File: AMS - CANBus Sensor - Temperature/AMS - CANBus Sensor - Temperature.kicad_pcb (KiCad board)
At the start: 2 copper layers, 72.9 x 71.1 mm, 45 parts, among them IC2 OPA4340UA, J1 Power_And_CAN, J2 Power_And_CAN, J3 TTL_Programmer, J4 ICSP, J5 Conn_01x02, J6 Screw_Terminal_01x02, Q1 IRF9Z34NPBF, U1 3568, U2 ATmega328P-P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

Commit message: wip for the temp sensor
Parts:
- removed IC2: OPA4340UA, SamacSys_Parts:SOIC127P600X175-14N
- removed J2: Power_And_CAN, TerminalBlock_Phoenix:TerminalBlock_Phoenix_MPT-0,5-4-2.54_1x04_P2.54mm_Horizontal
- removed J6: Screw_Terminal_01x02, TerminalBlock_Phoenix:TerminalBlock_Phoenix_MPT-0,5-2-2.54_1x02_P2.54mm_Horizontal
- removed R10, R11, R12, R13: 47K, Resistor_SMD:R_1206_3216Metric_Pad1.30x1.75mm_HandSolder
- removed R14, R15, R8, R9: 100K, Resistor_SMD:R_1206_3216Metric_Pad1.30x1.75mm_HandSolder
- removed RV1, RV2, RV3, RV4: 200k, Potentiometer_THT:Potentiometer_Bourns_3296W_Vertical
- removed U1: 3568, SamacSys_Parts:3568
- added C41: 0.33uF, Capacitor_SMD:C_1206_3216Metric_Pad1.33x1.80mm_HandSolder, F.Cu at (79.3, 73.2)
- added C42: 0.33uF, Capacitor_SMD:C_1206_3216Metric_Pad1.33x1.80mm_HandSolder, F.Cu at (79.3, 76.6)
- added C43: 100nF, Capacitor_SMD:C_1206_3216Metric_Pad1.33x1.80mm_HandSolder, F.Cu at (79.3, 79.9)
- added IC18: MAX31865AAP+, SamacSys_Parts:SOP65P778X199-20N, F.Cu at (87.4, 76.0)
- added J28: Conn_01x02, Connector_PinHeader_2.54mm:PinHeader_1x02_P2.54mm_Vertical, F.Cu at (84.6, 82.8)
- added J29: Conn_01x03, Connector_PinHeader_2.54mm:PinHeader_1x03_P2.54mm_Vertical, F.Cu at (78.6, 83.9)
- added J30: Conn_01x02, Connector_PinHeader_2.54mm:PinHeader_1x02_P2.54mm_Vertical, F.Cu at (89.3, 82.8)
- added R60: 430, Resistor_THT:R_Axial_DIN0207_L6.3mm_D2.5mm_P2.54mm_Vertical, F.Cu at (84.3, 89.7)
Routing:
- net GND: track 276.6 -> 0.00 mm, vias 2 -> 0
- net +5V: track 185.4 -> 0.00 mm, vias 2 -> 0
- net /BufferedADC/ADCIN4: track 98.9 -> 0.00 mm, vias 1 -> 0
- net /BareMinAtmel328P/PB3-D11-MOSI: track 98.5 -> 0.00 mm, vias 1 -> 0
- net /BareMinAtmel328P/PB1-D9: track 92.8 -> 0.00 mm, vias 2 -> 0
- net /BareMinAtmel328P/RESET: track 92.4 -> 0.00 mm, vias 4 -> 0
- net /BareMinAtmel328P/PC3-A3: track 78.5 -> 0.00 mm, vias 2 -> 0
- net Net-(U3-OSC1): track 77.0 -> 0.00 mm
- net /BareMinAtmel328P/PB5-D13-SCK: track 75.2 -> 0.00 mm, vias 2 -> 0
- net Net-(U3-OSC2): track 72.5 -> 0.00 mm
- net /BufferedADC/ADCIN3: track 58.3 -> 0.00 mm, vias 1 -> 0
- net /BareMinAtmel328P/PB4-D12-MISO: track 53.7 -> 0.00 mm, vias 2 -> 0
- net /BareMinAtmel328P/PC1-A1: track 51.2 -> 0.00 mm, vias 2 -> 0
- net /BareMinAtmel328P/PC2-A2: track 46.0 -> 0.00 mm, vias 3 -> 0
- net /BufferedADC/ADCIN2: track 45.2 -> 0.00 mm, vias 2 -> 0
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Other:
- board text added: "AMS CANBus RTD Temp V1.0 Rev A"
- board text removed: "1 Amp 5V"
- board text removed: "AMS CANBus Voltage V1.0 Rev A"
- board text removed: "Fused"

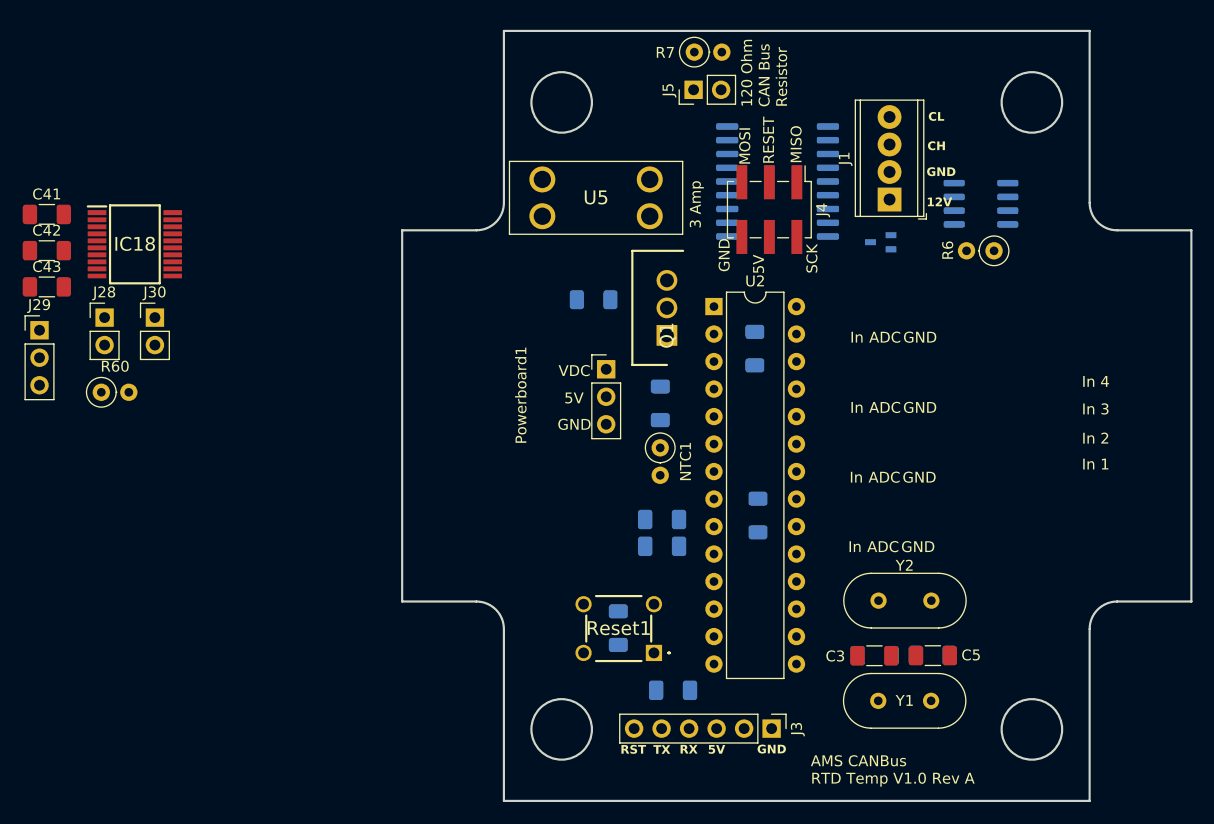
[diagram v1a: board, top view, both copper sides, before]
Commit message: Temp Sensor Done
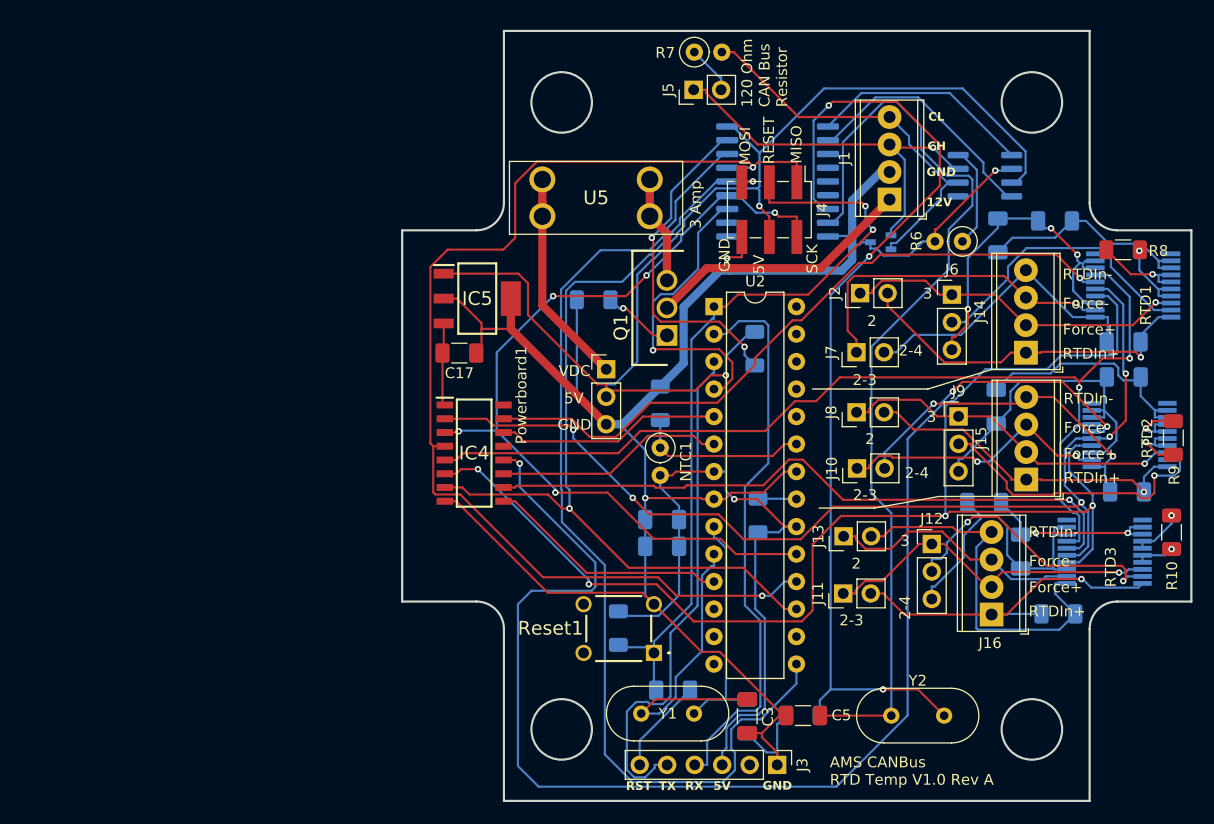
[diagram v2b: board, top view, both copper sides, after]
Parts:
- removed C41, C42: 0.33uF, Capacitor_SMD:C_1206_3216Metric_Pad1.33x1.80mm_HandSolder
- removed C43: 100nF, Capacitor_SMD:C_1206_3216Metric_Pad1.33x1.80mm_HandSolder
- removed IC18: MAX31865AAP+, SamacSys_Parts:SOP65P778X199-20N
- removed J28, J30: Conn_01x02, Connector_PinHeader_2.54mm:PinHeader_1x02_P2.54mm_Vertical
- removed J29: Conn_01x03, Connector_PinHeader_2.54mm:PinHeader_1x03_P2.54mm_Vertical
- removed R60: 430, Resistor_THT:R_Axial_DIN0207_L6.3mm_D2.5mm_P2.54mm_Vertical
- added C10: 100nF, Capacitor_SMD:C_1206_3216Metric_Pad1.33x1.80mm_HandSolder, B.Cu at (178.8, 85.0)
- added C11: 0.33uF, Capacitor_SMD:C_1206_3216Metric_Pad1.33x1.80mm_HandSolder, B.Cu at (178.8, 88.3)
- added C12: 0.33uF, Capacitor_SMD:C_1206_3216Metric_Pad1.33x1.80mm_HandSolder, B.Cu at (167.0, 91.0)
- added C13: 100nF, Capacitor_SMD:C_1206_3216Metric_Pad1.33x1.80mm_HandSolder, B.Cu at (179.1, 98.9)
- added C14: 0.33uF, Capacitor_SMD:C_1206_3216Metric_Pad1.33x1.80mm_HandSolder, B.Cu at (165.9, 99.9)
- added C15: 0.33uF, Capacitor_SMD:C_1206_3216Metric_Pad1.33x1.80mm_HandSolder, B.Cu at (169.3, 104.4)
- added C16: 100nF, Capacitor_SMD:C_1206_3216Metric_Pad1.33x1.80mm_HandSolder, B.Cu at (172.7, 110.1)
- added C17: 22uf, Capacitor_SMD:C_1206_3216Metric_Pad1.33x1.80mm_HandSolder, F.Cu at (117.4, 86.1)
- added C8: 0.33uF, Capacitor_SMD:C_1206_3216Metric_Pad1.33x1.80mm_HandSolder, B.Cu at (167.2, 75.2)
- added C9: 0.33uF, Capacitor_SMD:C_1206_3216Metric_Pad1.33x1.80mm_HandSolder, B.Cu at (172.4, 73.8)
- added IC1: MAX31865AAP+, SamacSys_Parts:SOP65P778X199-20N, B.Cu at (179.7, 79.8)
- added IC2: MAX31865AAP+, SamacSys_Parts:SOP65P778X199-20N, B.Cu at (179.3, 93.6)
- added IC3: MAX31865AAP+, SamacSys_Parts:SOP65P778X199-20N, B.Cu at (177.0, 104.4)
- added IC4: CD74HC4050ME4, SamacSys_Parts:SOIC127P600X175-16N, F.Cu at (118.8, 95.3)
- added IC5: AZ1117CH2-3.3TRG1, SamacSys_Parts:SOT230P700X180-4N, F.Cu at (119.1, 81.0)
- added J10: Conn_01x02, Connector_PinHeader_2.54mm:PinHeader_1x02_P2.54mm_Vertical, F.Cu at (154.1, 96.7)
- added J11: Conn_01x02, Connector_PinHeader_2.54mm:PinHeader_1x02_P2.54mm_Vertical, F.Cu at (152.9, 108.3)
- added J12: Conn_01x03, Connector_PinHeader_2.54mm:PinHeader_1x03_P2.54mm_Vertical, F.Cu at (161.0, 103.7)
- added J13: Conn_01x02, Connector_PinHeader_2.54mm:PinHeader_1x02_P2.54mm_Vertical, F.Cu at (152.9, 103.0)
- added J14: RTD1, TerminalBlock_Phoenix:TerminalBlock_Phoenix_MPT-0,5-4-2.54_1x04_P2.54mm_Horizontal, F.Cu at (169.7, 86.0)
- added J15: RTD2, TerminalBlock_Phoenix:TerminalBlock_Phoenix_MPT-0,5-4-2.54_1x04_P2.54mm_Horizontal, F.Cu at (169.8, 97.7)
- added J16: RTD3, TerminalBlock_Phoenix:TerminalBlock_Phoenix_MPT-0,5-4-2.54_1x04_P2.54mm_Horizontal, F.Cu at (166.6, 110.2)
- added J2: Conn_01x02, Connector_PinHeader_2.54mm:PinHeader_1x02_P2.54mm_Vertical, F.Cu at (154.4, 80.5)
- added J6: Conn_01x03, Connector_PinHeader_2.54mm:PinHeader_1x03_P2.54mm_Vertical, F.Cu at (162.9, 80.7)
- added J7: Conn_01x02, Connector_PinHeader_2.54mm:PinHeader_1x02_P2.54mm_Vertical, F.Cu at (154.1, 86.0)
- added J8: Conn_01x02, Connector_PinHeader_2.54mm:PinHeader_1x02_P2.54mm_Vertical, F.Cu at (154.1, 91.5)
- added J9: Conn_01x03, Connector_PinHeader_2.54mm:PinHeader_1x03_P2.54mm_Vertical, F.Cu at (163.5, 91.9)
- added R10: 430, Resistor_SMD:R_1206_3216Metric_Pad1.30x1.75mm_HandSolder, F.Cu at (183.2, 102.6)
- added R8: 430, Resistor_SMD:R_1206_3216Metric_Pad1.30x1.75mm_HandSolder, F.Cu at (178.7, 76.5)
- added R9: 430, Resistor_SMD:R_1206_3216Metric_Pad1.30x1.75mm_HandSolder, F.Cu at (183.4, 93.9)
- moved Y1 21.9 mm to (134.2, 119.4)
- moved C4 13.2 mm to (149.1, 119.5)
- moved C5 13.2 mm to (149.2, 119.5)
- moved C2 13.0 mm to (144.0, 119.6), turned to -90 degrees
- moved C3 13.0 mm to (144.0, 119.6), turned to -90 degrees
- moved Y2 10.7 mm to (157.3, 119.5)
- moved J3 3.39 mm to (146.8, 124.1)
- moved R6 3.04 mm to (163.9, 75.7)
- moved U4 2.62 mm to (166.0, 69.7)
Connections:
- net /BareMinAtmel328P/PB3-D11-MOSI renamed MOSI
- net /BareMinAtmel328P/PB4-D12-MISO renamed MISO
- net /BareMinAtmel328P/PB5-D13-SCK renamed CLK
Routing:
- net GND: track 0.00 -> 196.5 mm, vias 0 -> 3
- net +5V: track 0.00 -> 183.8 mm, vias 0 -> 3
- net /MAX31865AAP+2/CS3v: track 0.00 -> 127.9 mm, vias 0 -> 3
- net /MAX31865AAP+1/MOSI3v: track 0.00 -> 123.9 mm, vias 0 -> 4
- net MISO: track 0.00 -> 105.6 mm, vias 0 -> 2
- net /MAX31865AAP+1/SLC3v: track 0.00 -> 98.2 mm, vias 0 -> 5
- net /MAX31865AAP+1/MISO3v: track 0.00 -> 95.9 mm, vias 0 -> 2
- net /BareMinAtmel328P/PB1-D9: track 0.00 -> 93.4 mm
- net Net-(U3-OSC2): track 0.00 -> 91.7 mm, vias 0 -> 3
- net Net-(U3-OSC1): track 0.00 -> 86.8 mm
- net CLK: track 0.00 -> 81.4 mm, vias 0 -> 5
- net MOSI: track 0.00 -> 80.3 mm, vias 0 -> 2
- net /BareMinAtmel328P/RESET: track 0.00 -> 71.7 mm, vias 0 -> 2
- net /MAX31865AAP+1/CS3v: track 0.00 -> 63.8 mm, vias 0 -> 1
- net /MAX31865AAP+3/CS3v: track 0.00 -> 61.4 mm, vias 0 -> 1
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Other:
- board text added: "2"
- board text added: "2-3"
- board text added: "2-4"
- board text added: "3"
- board text added: "Force+"
- board text added: "Force-"
- board text added: "RTD1"
- board text added: "RTD2"
- board text added: "RTD3"
- board text added: "RTDIn+"
- board text added: "RTDIn-"
- board text removed: "ADC"
- board text removed: "In"
- board text removed: "In 1"
- board text removed: "In 2"
- board text removed: "In 3"
- board text removed: "In 4"

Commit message: Temperature Sensor board 1.0 REV. B
flipped the 3.3v and op amp to the back of the board to make assembly on a hotplate easier for the harder to place and solder components.
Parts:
- C17, IC4, IC5: moved to B.Cu
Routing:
- net CLK: track 81.4 -> 124.2 mm
- net +3.3V: track 7.67 -> 26.8 mm
- net GND: track 196.5 -> 180.0 mm, vias 3 -> 4
- net /MAX31865AAP+3/CS3v: track 61.4 -> 73.8 mm, vias 1 -> 4
- net MISO: track 105.6 -> 117.2 mm, vias 2 -> 8
- net /BareMinAtmel328P/PD5-D5: track 22.5 -> 32.8 mm, vias 0 -> 3
- net /MAX31865AAP+1/MOSI3v: track 123.9 -> 133.4 mm, vias 4 -> 5
- net /BareMinAtmel328P/PD3-D3: track 20.7 -> 28.2 mm, vias 0 -> 1
- net +5V: track 183.8 -> 178.0 mm, vias 3 -> 4
- net /MAX31865AAP+1/CS3v: track 63.8 -> 69.4 mm, vias 1 -> 4
- net MOSI: track 80.3 -> 83.9 mm, vias 2 -> 4
- net /MAX31865AAP+1/SLC3v: track 98.2 -> 95.1 mm, vias 5 -> 4
- net /BareMinAtmel328P/PD4-D4: track 21.2 -> 22.8 mm, vias 0 -> 1
- net /MAX31865AAP+2/RTDin-: track 32.0 -> 30.4 mm
- net CANBUS_L: track 35.8 -> 37.3 mm
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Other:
- board text added: "AMS CANBus RTD Temp V1.0 Rev B"
- board text removed: "AMS CANBus RTD Temp V1.0 Rev A"

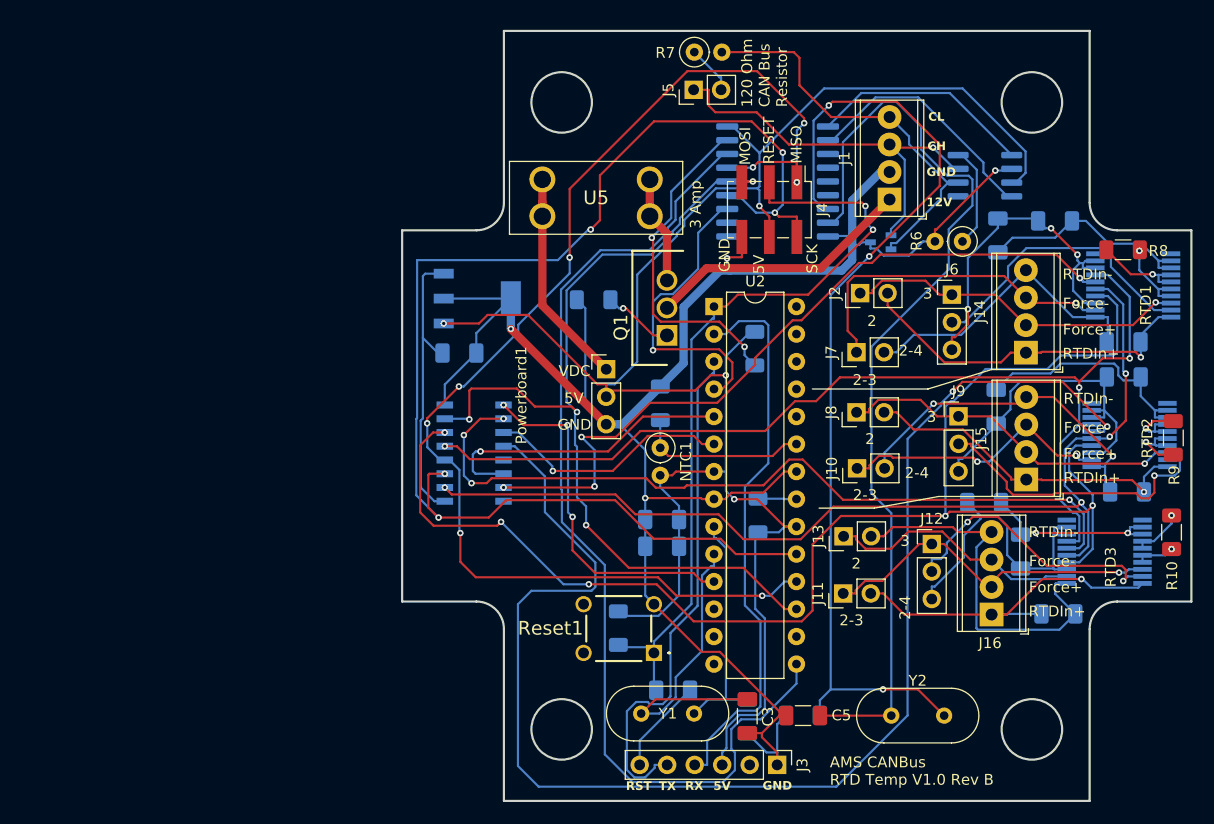
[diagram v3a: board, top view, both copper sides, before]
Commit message: Temperature Board v1.0 Rev C.
fixing my other dyslexic fuck up for the power on this board as well
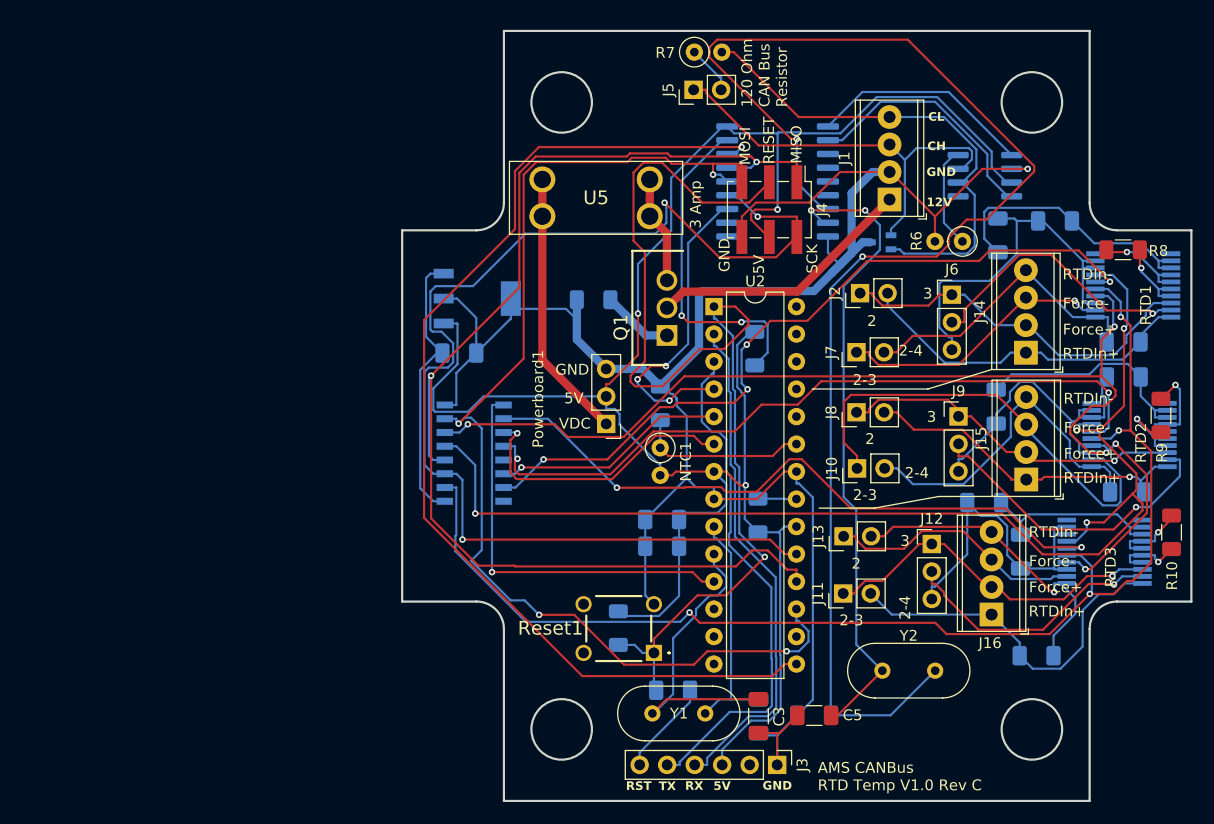
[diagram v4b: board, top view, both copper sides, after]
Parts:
- moved Powerboard1 5.05 mm to (131.0, 92.6), turned to 180 degrees
- moved C16 4.35 mm to (170.7, 114.0)
- moved Y2 4.23 mm to (156.5, 115.4)
- moved R9 2.36 mm to (182.2, 91.8)
- moved C3 1.03 mm to (145.0, 119.6)
- moved C4 1.03 mm to (150.2, 119.5)
- moved C2 1.03 mm to (145.0, 119.6)
- moved C5 1.03 mm to (150.2, 119.5)
- moved Y1 1.03 mm to (135.2, 119.3)
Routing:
- net /MAX31865AAP+2/CS3v: track 129.1 -> 67.4 mm
- net Net-(U3-OSC2): track 91.3 -> 129.6 mm, vias 3 -> 2
- net /BareMinAtmel328P/RESET: track 71.1 -> 99.9 mm, vias 2 -> 1
- net /MAX31865AAP+1/MOSI3v: track 133.4 -> 105.9 mm
- net Net-(U3-OSC1): track 86.3 -> 59.0 mm, vias 0 -> 2
- net MOSI: track 83.9 -> 107.4 mm
- net /MAX31865AAP+1/SLC3v: track 95.1 -> 115.3 mm
- net /MAX31865AAP+2/FORCE-: track 25.3 -> 42.3 mm, vias 2 -> 0
- net /MAX31865AAP+1/MISO3v: track 96.3 -> 112.0 mm, vias 3 -> 4
- net CLK: track 124.2 -> 109.3 mm, vias 5 -> 3
- net GND: track 180.0 -> 194.7 mm, vias 4 -> 1
- net /MAX31865AAP+3/CS3v: track 73.8 -> 62.3 mm, vias 4 -> 2
- net +5V: track 178.0 -> 188.8 mm, vias 4 -> 3
- net CANBUS_L: track 37.3 -> 45.4 mm
- net /MAX31865AAP+3/RTDin-: track 35.6 -> 28.5 mm, vias 0 -> 1
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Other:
- board text added: "AMS CANBus RTD Temp V1.0 Rev C"
- board text removed: "AMS CANBus RTD Temp V1.0 Rev B"
